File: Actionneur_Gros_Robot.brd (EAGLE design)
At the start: 110 x 55 mm, 52 parts, among them M1 ARDUINO-NANO-3.0, M10 SERVO, M11 SERVO, M2 SERVO, M3 SERVO, M4 SERVO, M5 SERVO, M6 SERVO, M7 SERVO, M8 SERVO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

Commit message: revA3
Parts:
- added R19: 15K, rcl:0207/7
- moved R2 0.40 mm to (27.9, 42.6)
- moved R1 0.40 mm to (26.2, 36.5)
- moved R3 0.40 mm to (30.3, 42.6)
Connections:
- new net N$15: R19.1, U$2.8
- net GND: now also R19.2
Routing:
- net N$15: track 0.00 -> 13.3 mm, vias 0 -> 2
- net VCC: track 216.3 -> 217.8 mm
- net GND: vias 21 -> 22

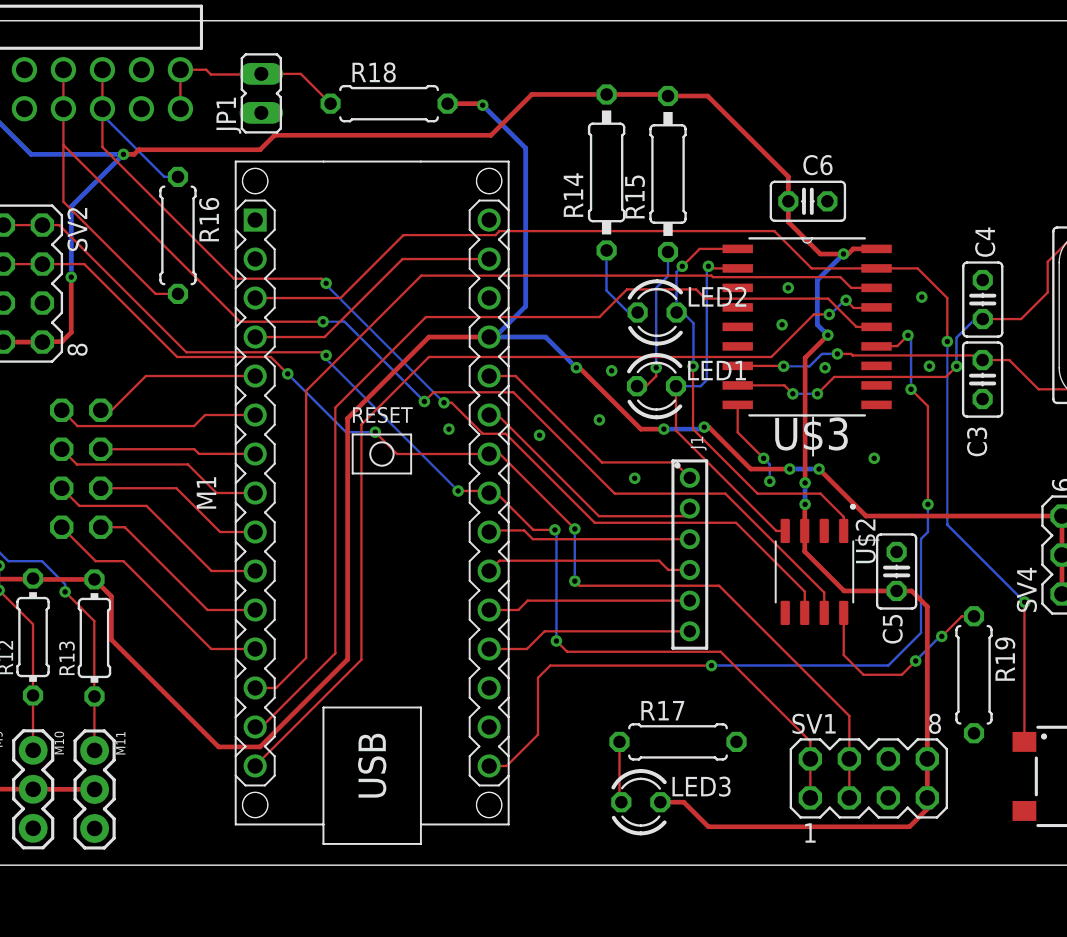
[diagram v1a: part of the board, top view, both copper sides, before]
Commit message: Added testpins for CANH and CANL
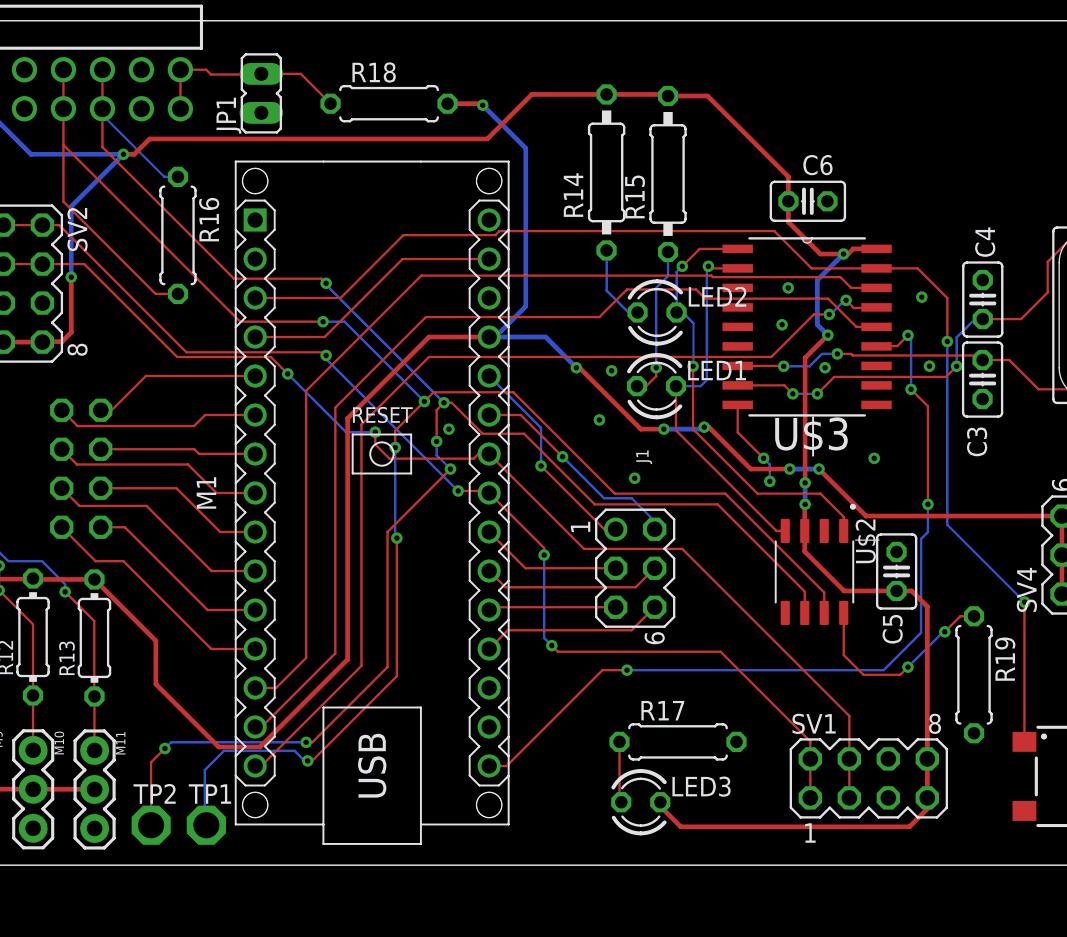
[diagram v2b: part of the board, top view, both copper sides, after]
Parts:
- added TP1, TP2: PTR1PAD1-17, testpad:P1-17
- J1: device Wurth_Connectors_WR-PHD:62000611121 -> con-lstb:MA03-2
- moved J1 3.67 mm to (74.5, 19.3)
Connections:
- net CANH: now also TP1.TP
- net CANL: now also TP2.TP
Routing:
- net CANL: track 71.2 -> 112.8 mm, vias 2 -> 6
- net CANH: track 82.0 -> 119.9 mm, vias 2 -> 5
- net N$3: track 13.3 -> 8.31 mm
- net N$4: track 13.3 -> 9.22 mm
- net SCK1: track 56.3 -> 54.2 mm
- net N$7: track 15.8 -> 13.8 mm, vias 0 -> 1
- net N$6: track 16.1 -> 14.2 mm, vias 0 -> 1
- net N$5: track 13.6 -> 11.7 mm
- net N$2: track 13.5 -> 11.9 mm
- net I2C_SCL: track 96.2 -> 94.9 mm, vias 4 -> 2
- net GND: vias 22 -> 21
